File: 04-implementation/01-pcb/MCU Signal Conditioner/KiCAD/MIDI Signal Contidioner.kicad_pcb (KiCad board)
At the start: 2 copper layers, 94.1 x 37 mm, 31 parts, among them J2 ARDUINO-CONN-8X2, J3 ARDUINO-CONN-8X2, U4 24CS01, U6 MCP1700-SOT89, X1 SSW-107-02-G-D, X2 SSW-107-02-G-D, X3 SSW-107-02-G-D, X4 SSW-107-02-G-D, X5 MINI-USB-SHIELD-32005-201, X6 USB-787616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

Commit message: Verified board-to-board pinouts are consistent.
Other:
- board text removed: "3. verify board-to-board connectors, etc. on checklist"

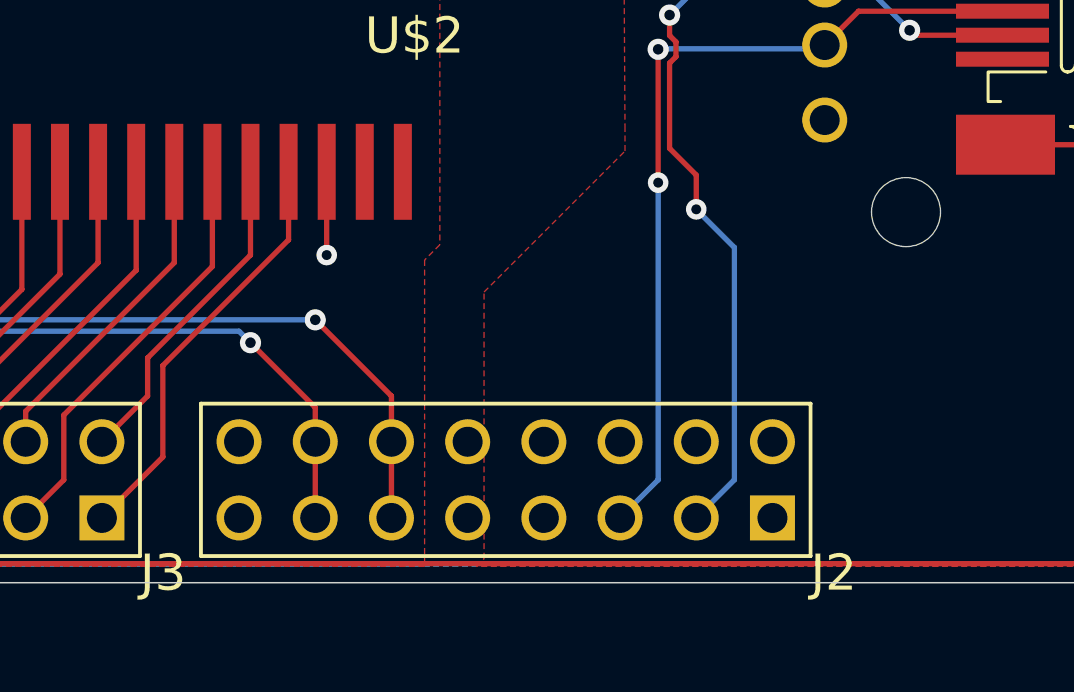
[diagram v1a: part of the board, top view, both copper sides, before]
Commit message: Update MCU Signal Conditioner PCB for placement compatibility with MCU PCB.
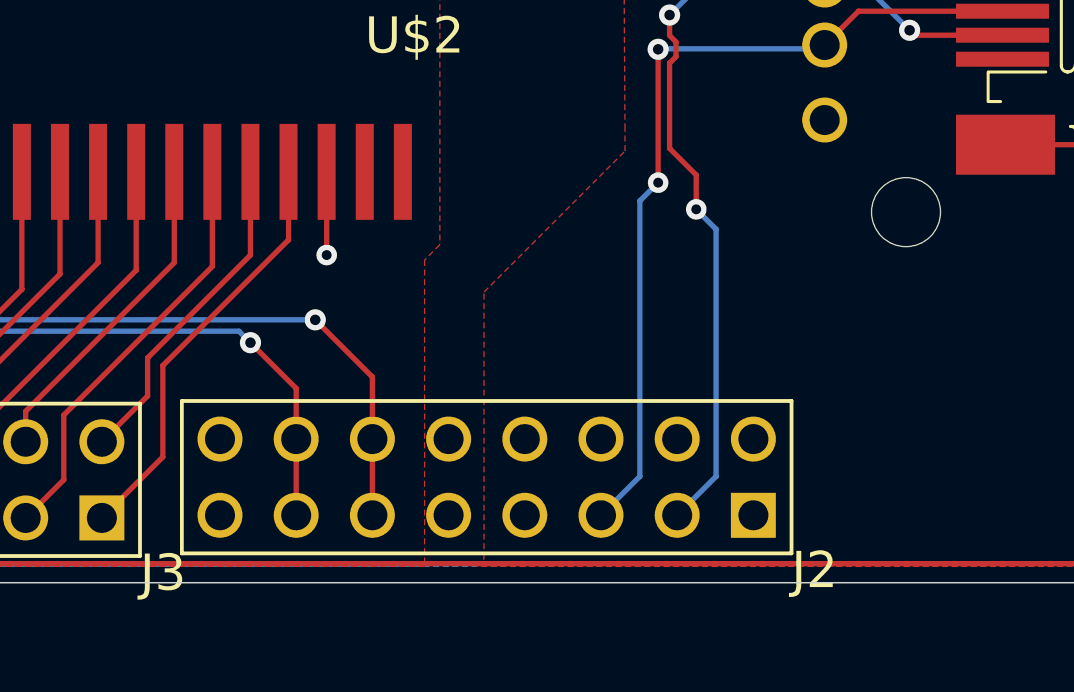
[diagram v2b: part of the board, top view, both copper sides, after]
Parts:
- moved J2 0.64 mm to (178.3, 121.2)
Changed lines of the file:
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@@
     (thickness 1.6)
     (drawings 12)
-    (tracks 465)
+    (tracks 466)
     (zones 0)
     (modules 31)
@@
   )
   (setup
-    (last_trace_width 0.25)
+    (last_trace_width 0.1778)
+    (user_trace_width 0.1778)
     (trace_clearance 0.1524)
     (zone_clearance 0.508)
@@
   )
   (module "MIDI Signal Contidioner:ARDUINO-CONN-8X2" (layer Top)
-    (at 178.9176 121.3231 180)
+    (at 178.2826 121.2342 180)
     (fp_text reference J2 (at -1.27 -2.54) (layer F.SilkS)
       (effects (font (size 1.2065 1.2065) (thickness 0.09652)) (justify left bottom))
@@
   (segment (start 121.8946 112.9411) (end 121.8946 113.9571) (width 0.1778) (layer Bottom) (net 5))
   (segment (start 137.0076 113.4491) (end 138.7856 113.4491) (width 0.1778) (layer Bottom) (net 5))
-  (segment (start 163.6776 121.3231) (end 163.6776 118.7831) (width 0.1778) (layer Top) (net 5))
-  (segment (start 163.6776 118.7831) (end 163.6776 117.6401) (width 0.1778) (layer Top) (net 5))
-  (segment (start 163.6776 117.6401) (end 161.5186 115.4811) (width 0.1778) (layer Top) (net 5))
   (via (at 161.5186 115.4811) (size 0.7056) (drill 0.35) (layers Top Bottom) (net 5))
   (segment (start 161.5186 115.4811) (end 161.1376 115.1001) (width 0.1778) (layer Bottom) (net 5))
@@
   (segment (start 126.5936 113.4491) (end 126.0856 112.9411) (width 0.1778) (layer Top) (net 5))
   (segment (start 138.7856 113.4491) (end 140.1826 113.4491) (width 0.1778) (layer Top) (net 5))
+  (segment (start 163.0426 121.2342) (end 163.0426 118.6942) (width 0.1778) (layer Top) (net 5))
+  (segment (start 163.0426 117.0051) (end 161.5186 115.4811) (width 0.1778) (layer Top) (net 5))
+  (segment (start 163.0426 118.6942) (end 163.0426 117.0051) (width 0.1778) (layer Top) (net 5))
   (via (at 124.4346 113.9571) (size 0.6858) (drill 0.3302) (layers Top Bottom) (net 6))
   (segment (start 124.4346 113.9571) (end 124.4346 111.7981) (width 0.1778) (layer Bottom) (net 6))
@@
   (segment (start 127.6096 111.7981) (end 130.5306 111.7981) (width 0.1778) (layer Top) (net 6))
   (via (at 130.5306 111.7981) (size 0.6858) (drill 0.3302) (layers Top Bottom) (net 6))
-  (segment (start 130.5306 111.7981) (end 139.5476 111.7981) (width 0.1778) (layer Bottom) (net 6))
-  (via (at 139.5476 111.7981) (size 0.6858) (drill 0.3302) (layers Top Bottom) (net 6))
   (segment (start 130.5306 107.2626) (end 130.5306 109.8931) (width 0.1778) (layer Top) (net 6))
   (via (at 130.5306 109.8931) (size 0.6858) (drill 0.3302) (layers Top Bottom) (net 6))
   (segment (start 130.5306 109.8931) (end 130.5306 111.7981) (width 0.1778) (layer Bottom) (net 6))
-  (segment (start 139.5476 111.7981) (end 140.5636 111.7981) (width 0.1778) (layer Top) (net 6))
-  (segment (start 166.2176 121.3231) (end 166.2176 118.7831) (width 0.1778) (layer Top) (net 6))
-  (segment (start 166.2176 118.7831) (end 166.2176 117.2591) (width 0.1778) (layer Top) (net 6))
-  (segment (start 166.2176 117.2591) (end 163.6776 114.7191) (width 0.1778) (layer Top) (net 6))
-  (via (at 163.6776 114.7191) (size 0.7056) (drill 0.35) (layers Top Bottom) (net 6))
-  (segment (start 163.6776 114.7191) (end 152.5016 114.7191) (width 0.1778) (layer Bottom) (net 6))
-  (segment (start 151.3586 113.5761) (end 150.9776 113.5761) (width 0.1778) (layer Bottom) (net 6))
-  (via (at 150.9776 113.5761) (size 0.7056) (drill 0.35) (layers Top Bottom) (net 6))
-  (segment (start 150.9776 113.5761) (end 147.4216 113.5761) (width 0.1778) (layer Top) (net 6))
-  (via (at 147.4216 113.5761) (size 0.7056) (drill 0.35) (layers Top Bottom) (net 6))
-  (segment (start 147.4216 113.5761) (end 141.7066 113.5761) (width 0.1778) (layer Bottom) (net 6))
-  (via (at 141.7066 113.5761) (size 0.7056) (drill 0.35) (layers Top Bottom) (net 6))
-  (segment (start 141.7066 113.5761) (end 141.7066 112.9411) (width 0.1778) (layer Top) (net 6))
-  (segment (start 141.7066 112.9411) (end 140.5636 111.7981) (width 0.1778) (layer Top) (net 6))
-  (segment (start 152.5016 114.7191) (end 151.3586 113.5761) (width 0.1778) (layer Bottom) (net 6))
   (segment (start 128.4986 121.3231) (end 128.4986 118.7831) (width 0.1778) (layer Top) (net 6))
   (segment (start 128.4986 118.7831) (end 128.4986 116.4971) (width 0.1778) (layer Top) (net 6))
@@
   (segment (start 128.6256 112.4331) (end 127.9906 111.7981) (width 0.1778) (layer Top) (net 6))
   (segment (start 127.9906 111.7981) (end 127.6096 111.7981) (width 0.1778) (layer Top) (net 6))
+  (segment (start 152.5016 114.7191) (end 151.3586 113.5761) (width 0.1778) (layer Bottom) (net 6))
+  (segment (start 141.7066 112.9411) (end 140.5636 111.7981) (width 0.1778) (layer Top) (net 6))
+  (segment (start 141.7066 113.5761) (end 141.7066 112.9411) (width 0.1778) (layer Top) (net 6))
+  (via (at 141.7066 113.5761) (size 0.7056) (drill 0.35) (layers Top Bottom) (net 6))
+  (segment (start 147.4216 113.5761) (end 141.7066 113.5761) (width 0.1778) (layer Bottom) (net 6))
+  (via (at 147.4216 113.5761) (size 0.7056) (drill 0.35) (layers Top Bottom) (net 6))
+  (segment (start 150.9776 113.5761) (end 147.4216 113.5761) (width 0.1778) (layer Top) (net 6))
+  (via (at 150.9776 113.5761) (size 0.7056) (drill 0.35) (layers Top Bottom) (net 6))
+  (segment (start 151.3586 113.5761) (end 150.9776 113.5761) (width 0.1778) (layer Bottom) (net 6))
+  (segment (start 163.6776 114.7191) (end 152.5016 114.7191) (width 0.1778) (layer Bottom) (net 6))
+  (via (at 163.6776 114.7191) (size 0.7056) (drill 0.35) (layers Top Bottom) (net 6))
+  (segment (start 139.5476 111.7981) (end 140.5636 111.7981) (width 0.1778) (layer Top) (net 6))
+  (via (at 139.5476 111.7981) (size 0.6858) (drill 0.3302) (layers Top Bottom) (net 6))
+  (segment (start 130.5306 111.7981) (end 139.5476 111.7981) (width 0.1778) (layer Bottom) (net 6))
+  (segment (start 165.5826 121.2342) (end 165.5826 118.6942) (width 0.1778) (layer Top) (net 6))
+  (segment (start 165.5826 116.6241) (end 163.6776 114.7191) (width 0.1778) (layer Top) (net 6))
+  (segment (start 165.5826 118.6942) (end 165.5826 116.6241) (width 0.1778) (layer Top) (net 6))
   (via (at 175.1076 110.1471) (size 0.6858) (drill 0.3302) (layers Top Bottom) (net 15))
   (segment (start 175.1076 105.7021) (end 175.1076 110.1471) (width 0.1778) (layer Top) (net 15))
@@
   (segment (start 186.5856 104.4321) (end 181.7865 104.4321) (width 0.1778) (layer Top) (net 15))
   (segment (start 181.7865 104.4321) (end 180.6595 105.5591) (width 0.1778) (layer Top) (net 15))
-  (segment (start 175.1076 120.0531) (end 173.8376 121.3231) (width 0.1778) (layer Bottom) (net 15))
-  (segment (start 175.1076 110.1471) (end 175.1076 120.0531) (width 0.1778) (layer Bottom) (net 15))
+  (segment (start 173.2026 121.2342) (end 174.498 119.9388) (width 0.1778) (layer Bottom) (net 15))
+  (segment (start 174.498 110.7567) (end 175.1076 110.1471) (width 0.1778) (layer Bottom) (net 15))
+  (segment (start 174.498 119.9388) (end 174.498 110.7567) (width 0.1778) (layer Bottom) (net 15))
   (via (at 176.3776 111.0361) (size 0.6858) (drill 0.3302) (layers Top Bottom) (net 16))
-  (segment (start 176.3776 121.3231) (end 177.6476 120.0531) (width 0.1778) (layer Bottom) (net 16))
-  (segment (start 176.3776 111.0361) (end 177.6476 112.3061) (width 0.1778) (layer Bottom) (net 16))
-  (segment (start 177.6476 112.3061) (end 177.6476 120.0531) (width 0.1778) (layer Bottom) (net 16))
   (segment (start 176.3776 111.0361) (end 176.3776 109.8931) (width 0.1778) (layer Top) (net 16))
   (segment (start 176.3776 109.8931) (end 175.4886 109.0041) (width 0.1778) (layer Top) (net 16))
@@
   (segment (start 183.4896 105.0671) (end 181.9816 103.5591) (width 0.1778) (layer Bottom) (net 16))
   (segment (start 181.9816 103.5591) (end 180.6595 103.5591) (width 0.1778) (layer Bottom) (net 16))
+  (segment (start 175.7426 121.2342) (end 177.038 119.9388) (width 0.1778) (layer Bottom) (net 16))
+  (segment (start 177.038 111.6965) (end 176.3776 111.0361) (width 0.1778) (layer Bottom) (net 16))
+  (segment (start 177.038 119.9388) (end 177.038 111.6965) (width 0.1778) (layer Bottom) (net 16))
   (segment (start 140.8541 109.5121) (end 142.3416 109.5121) (width 0.1778) (layer Top) (net 18))
   (via (at 142.3416 109.5121) (size 0.6858) (drill 0.3302) (layers Top Bottom) (net 18))
